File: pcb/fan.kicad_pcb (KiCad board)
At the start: 2 copper layers, 212.8 x 143.6 mm, 59 parts, among them J1 MJ-4PP-9, J2 Conn_01x01_Female, J3 Conn_01x01_Female, SW1 SW_PUSH-kbd, SW10 SW_PUSH-kbd, SW11 SW_PUSH-kbd, SW12 SW_PUSH-kbd, SW13 SW_PUSH-kbd, SW14 SW_PUSH-kbd, SW15 SW_PUSH-kbd, SW16 SW_PUSH-kbd, SW17 SW_PUSH-kbd, SW18 SW_PUSH-kbd, SW19 SW_PUSH-kbd, SW2 SW_PUSH-kbd, SW20 SW_PUSH-kbd, SW21 SW_PUSH-kbd, SW22 SW_PUSH-kbd, SW23 SW_PUSH-kbd, SW24 SW_PUSH-kbd, SW25 SW_PUSH-kbd, SW26 SW_PUSH-kbd, SW27 SW_PUSH-kbd, SW28 SW_PUSH-kbd, SW29 SW_PUSH-kbd, SW3 SW_PUSH-kbd, SW30 SW_PUSH-kbd, SW31 SW_PUSH-kbd, SW32 SW_PUSH-kbd, SW33 SW_PUSH-kbd, SW34 SW_PUSH-kbd, SW35 SW_PUSH-kbd, SW36 SW_PUSH-kbd, SW37 SW_PUSH-kbd, SW38 SW_PUSH-kbd, SW39 SW_PUSH-kbd, SW4 SW_PUSH-kbd, SW40 SW_PUSH-kbd, SW41 SW_PUSH, SW5 SW_PUSH-kbd, SW6 SW_PUSH-kbd, SW7 SW_PUSH-kbd, SW8 SW_PUSH-kbd, SW9 SW_PUSH-kbd, U1 BluePill_STM32F103C

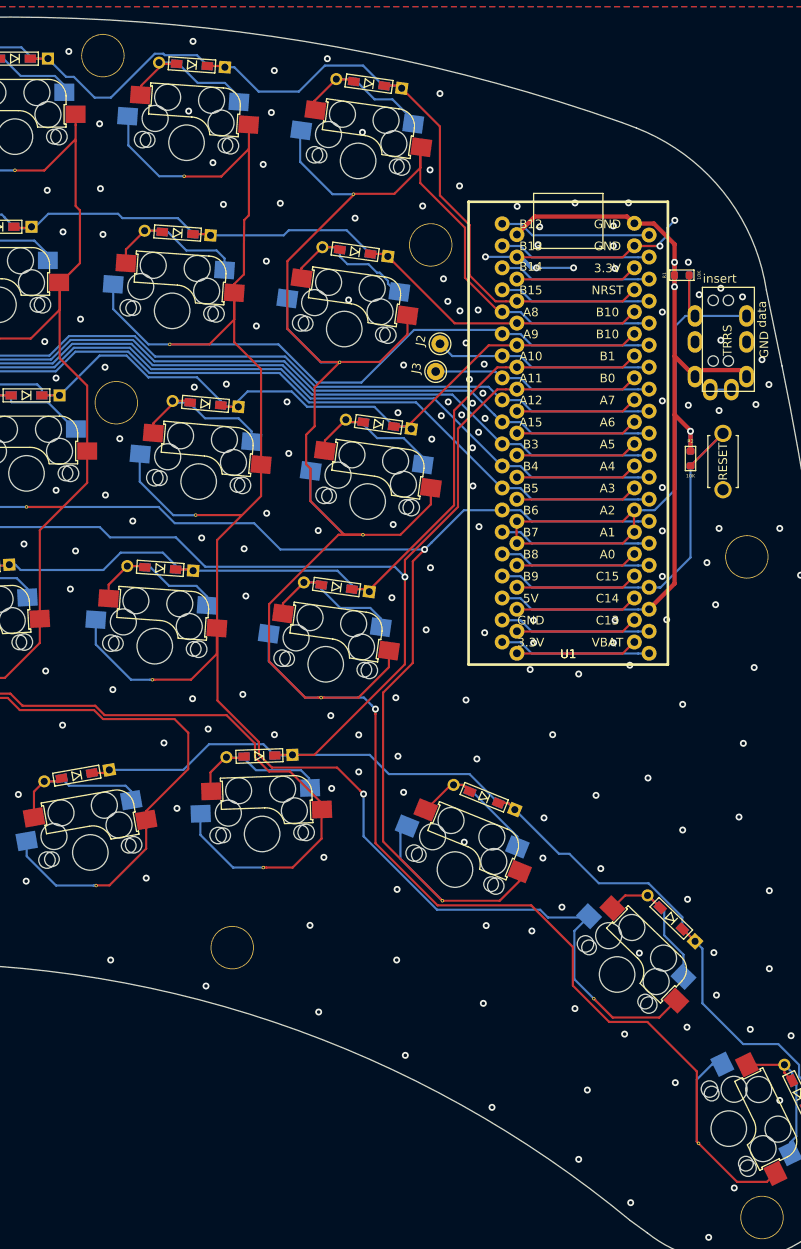
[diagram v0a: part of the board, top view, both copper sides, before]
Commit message: JLPCB出した後だけど回路のエラーあったので修正した 寝落ち寸前に出すものではない..._(:3 」∠ )_
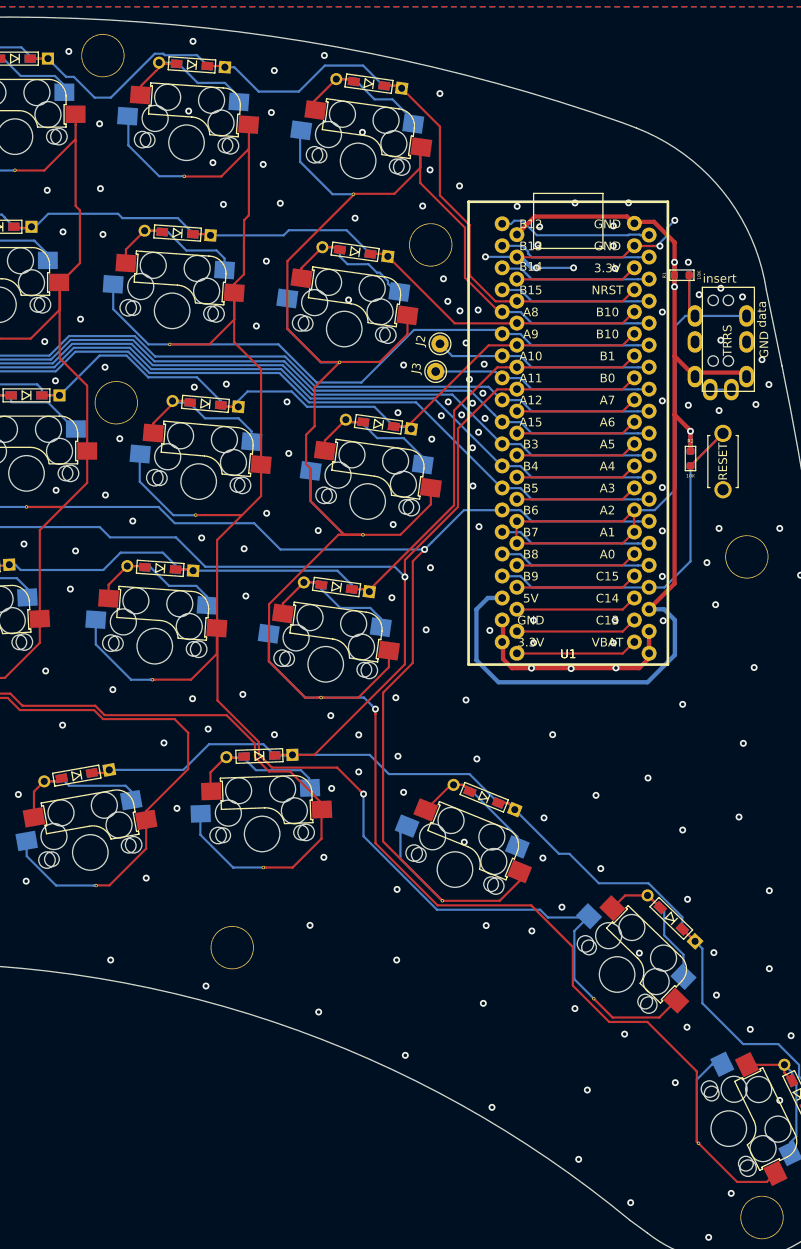
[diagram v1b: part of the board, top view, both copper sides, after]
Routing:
- net VCC: track 101.3 -> 125.9 mm
- net GND: track 69.2 -> 59.7 mm
